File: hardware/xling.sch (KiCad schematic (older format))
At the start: 57 parts

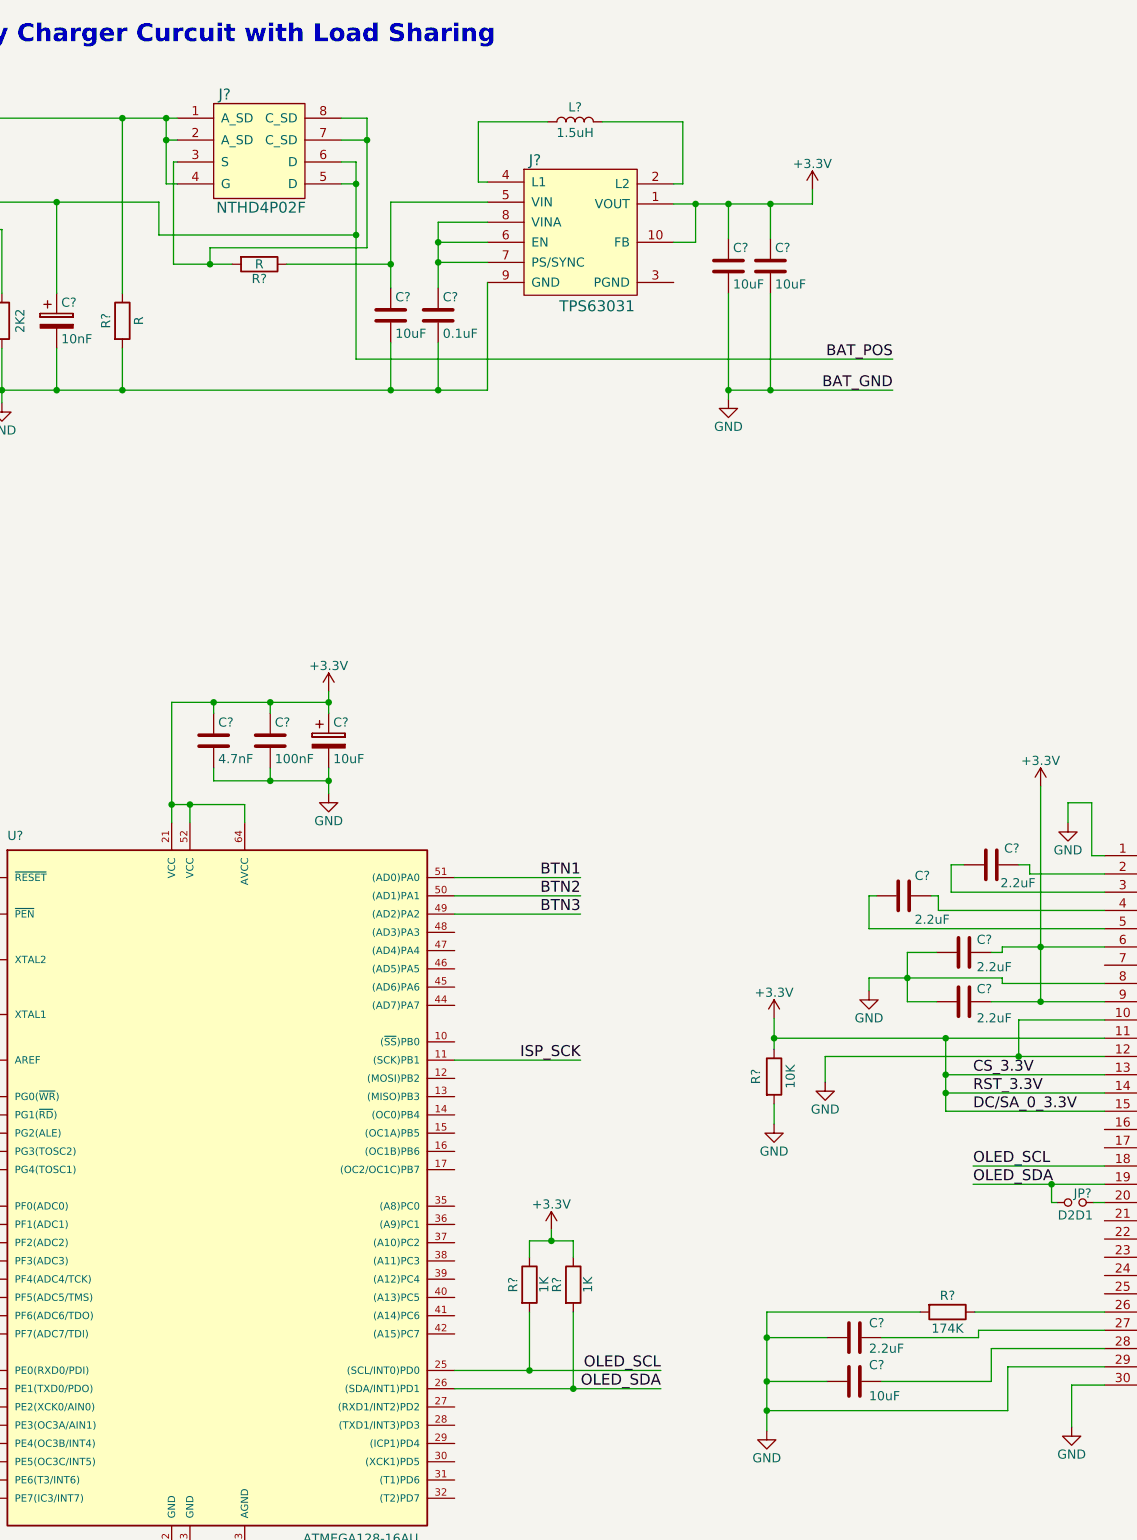
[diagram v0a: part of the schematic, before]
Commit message: patch 0.1.1: Add missing component values in schematic.
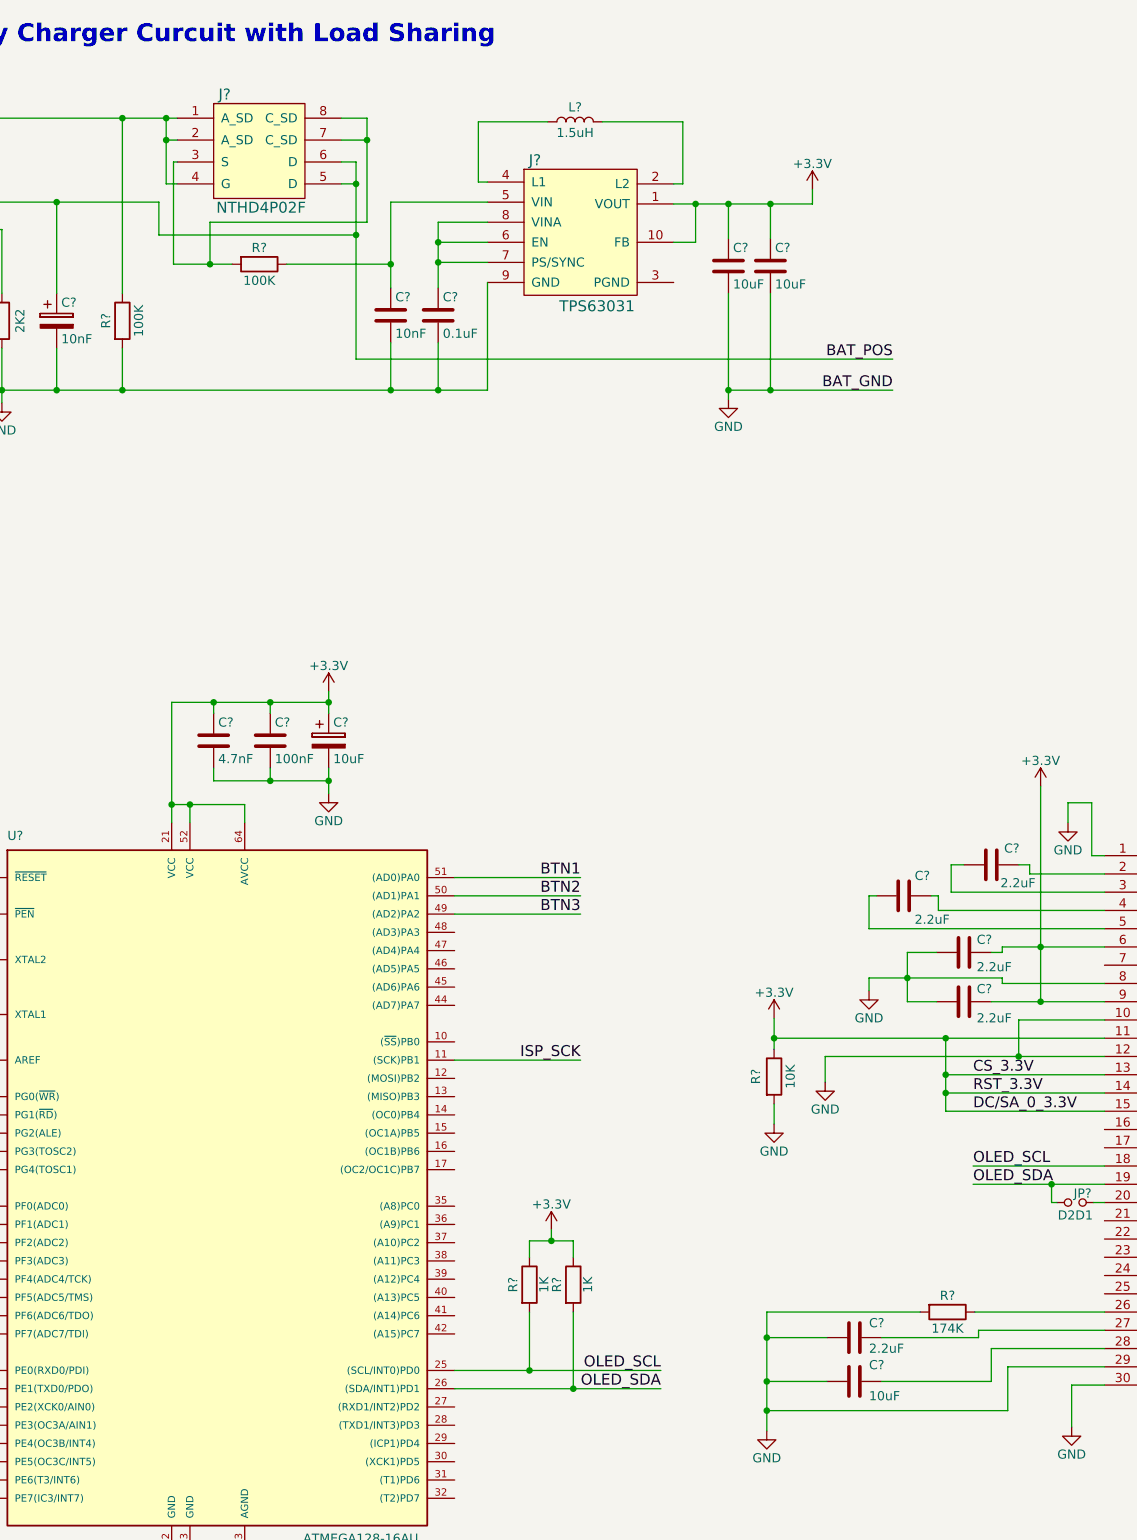
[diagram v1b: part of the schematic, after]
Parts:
- C?: value 10uF -> 10nF
- R? (x2): value R -> 100K

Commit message: patch 0.1.2: Schematic update with assigned footprints.
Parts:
- added J6: Battery, Pin_Headers:Pin_Header_Straight_1x02, symbol Conn_01x02
- C1, C17, C2, C9: renamed from C?; footprint (none) -> Capacitors_SMD:C_0805
- C10, C11, C12, C14, C16: renamed from C?; footprint (none) -> Capacitors_SMD:C_0603
- C13, C15, C18, C19, C20, C4, C7: renamed from C?; footprint (none) -> Capacitors_SMD:C_0402
- C3, C6: renamed from C?; value 10nF -> 4.7uF; footprint (none) -> Capacitors_SMD:CP_Elec_10x10
- C5, C8: renamed from C?; footprint (none) -> Capacitors_SMD:C_0201
- D1: renamed from D?; footprint (none) -> LEDs:LED_0603
- D2, D3: renamed from D?; footprint (none) -> LEDs:LED_0805
- D4: renamed from D?; value yellow -> amber; footprint (none) -> LEDs:LED_0603
- J4: renamed from J?; footprint (none) -> Connectors:USB_Mini-B
- J5: renamed from J?; footprint (none) -> Socket_Strips:Socket_Strip_Angled_2x03_Pitch2.54mm
- L1: renamed from L?; footprint (none) -> Inductors_SMD:L_1210
- R1, R17, R18, R19, R2, R3, R4, R5, R6, R7: renamed from R?; footprint (none) -> Resistors_SMD:R_1206
- R10: renamed from R?; footprint (none) -> Resistors_SMD:R_0805
- R11, R12, R13, R14, R15, R16, R8, R9: renamed from R?; footprint (none) -> Resistors_SMD:R_0603
- SW1, SW2, SW3, SW4: renamed from SW?; footprint (none) -> Buttons_Switches_THT:SW_PUSH_6mm
- gave numbers to parts that had none: 7
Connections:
- net GND: now also J6.2 (Pin_2)
- net BAT_POS: no longer names the net of C6.1, J1.5 (D), J1.6 (D), J3.3 (VBAT)
- net BAT_POS: now also J6.1 (Pin_1)

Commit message: patch 0.1.3: Add library with footprints.
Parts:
- JP1: footprint (none) -> Pin_Headers:Pin_Header_Straight_1x02
- Y1: footprint (none) -> Crystals:Crystal_HC49-SD_SMD
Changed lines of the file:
@@
 Title "Xling (Virtual Monster) Schematic"
 Date ""
-Rev "0.1.2"
+Rev "0.1.3"
 Comp ""
 Comment1 ""
@@
 F 0 "Y1" V 3060 6070 50  0000 C CNN
 F 1 "8MHz" V 2830 5830 50  0000 C CNN
-F 2 "" H 2840 6070 50  0001 C CNN
+F 2 "Crystals:Crystal_HC49-SD_SMD" H 2840 6070 50  0001 C CNN
 F 3 "" H 2840 6070 50  0001 C CNN
 	1    2840 6070
@@
 F 0 "JP1" H 9270 7200 50  0000 C CNN
 F 1 "D2D1" H 9310 7320 50  0000 C CNN
-F 2 "" H 9310 7250 50  0001 C CNN
+F 2 "Pin_Headers:Pin_Header_Straight_1x02" H 9310 7250 50  0001 C CNN
 F 3 "" H 9310 7250 50  0001 C CNN
 	1    9310 7250

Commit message: patch 0.1.4: Add footprint for MCP73831.
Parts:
- J3: footprint (none) -> Xling Footprints:MCP73831_SOT_23
- U1: footprint (none) -> Xling Footprints:Connector_FFC_FPC_MOLEX_524353071_30-pins
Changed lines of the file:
@@
 Title "Xling (Virtual Monster) Schematic"
 Date ""
-Rev "0.1.3"
+Rev "0.1.4"
 Comp ""
 Comment1 ""
@@
 F 0 "J3" H 2620 2220 60  0000 C CNN
 F 1 "MCP73831" H 2820 1620 60  0000 C CNN
-F 2 "" H 2820 1920 60  0001 C CNN
+F 2 "Xling Footprints:MCP73831_SOT_23" H 2820 1920 60  0001 C CNN
 F 3 "" H 2820 1920 60  0001 C CNN
 	1    2820 1920
@@
 F 0 "U1" H 9730 8200 60  0000 C CNN
 F 1 "SH1106G" H 11200 4990 60  0000 C CNN
-F 2 "" H 10820 7000 60  0001 C CNN
+F 2 "Xling Footprints:Connector_FFC_FPC_MOLEX_524353071_30-pins" H 10820 7000 60  0001 C CNN
 F 3 "" H 10820 7000 60  0001 C CNN
 	1    10520 6700

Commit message: patch 0.1.5: Add footprint for TPS63031.
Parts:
- J2: footprint (none) -> Xling Footprints:TPS63031_QFN_10
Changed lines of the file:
@@
 Title "Xling (Virtual Monster) Schematic"
 Date ""
-Rev "0.1.4"
+Rev "0.1.5"
 Comp ""
 Comment1 ""
@@
 F 0 "J2" H 6350 2260 60  0000 C CNN
 F 1 "TPS63031" H 6690 1460 60  0000 C CNN
-F 2 "" H 6470 1610 60  0001 C CNN
+F 2 "Xling Footprints:TPS63031_QFN_10" H 6470 1610 60  0001 C CNN
 F 3 "" H 6470 1610 60  0001 C CNN
 	1    6540 1900

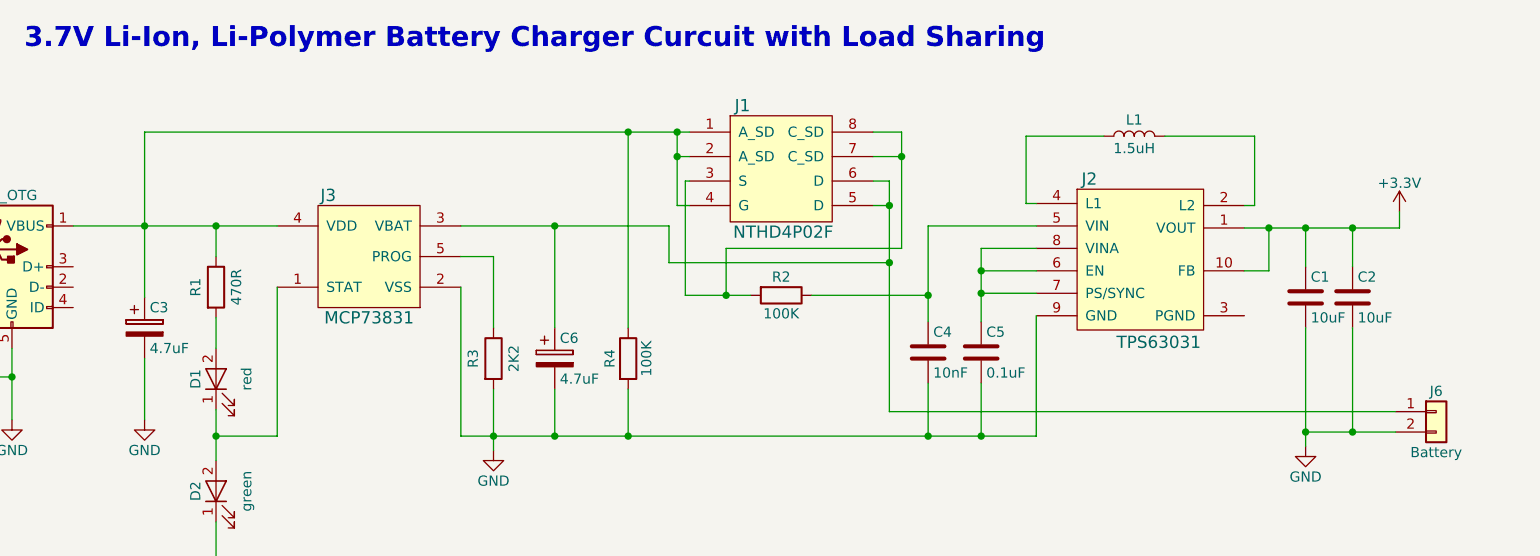
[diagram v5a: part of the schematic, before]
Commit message: patch 0.1.6: Add footprint for ATmega128L.
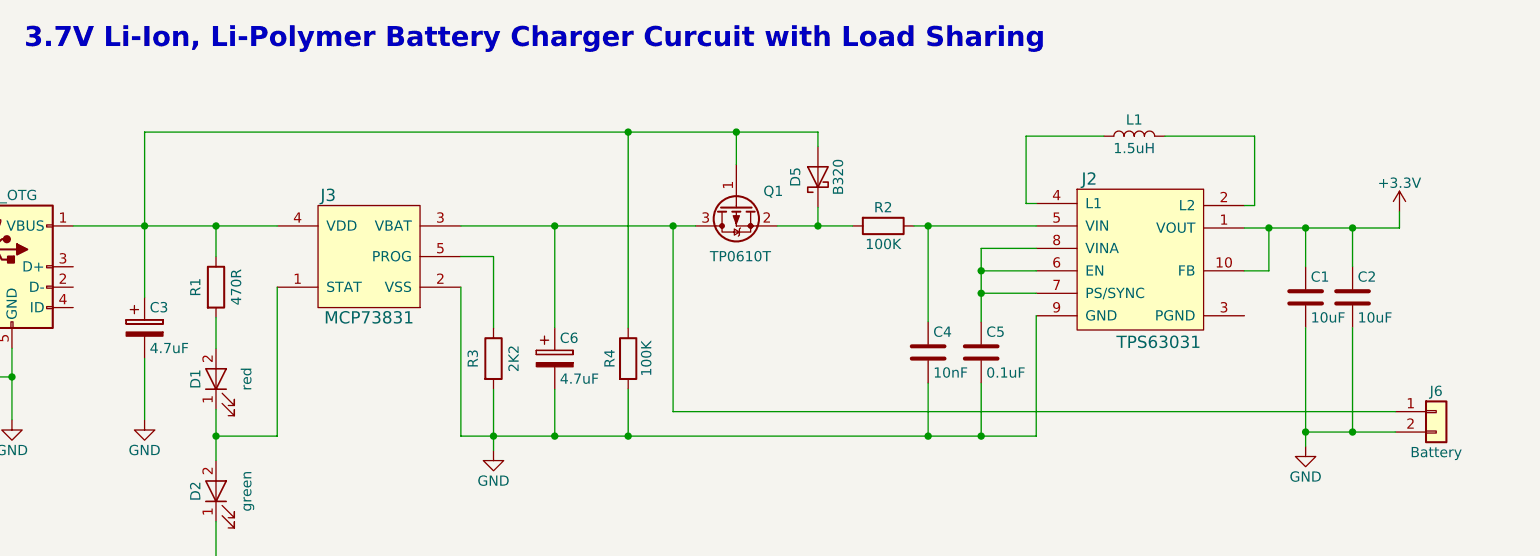
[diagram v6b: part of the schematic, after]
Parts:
- removed J1: NTHD4P02F, symbol NTHD4P02F
- added D5: B320, Diodes_SMD:SMC_Standard, symbol B320
- added Q1: TP0610T, TO_SOT_Packages_SMD:SOT-23, symbol TP0610T
- U2: footprint TQFP64 -> Xling Footprints:ATmega128_64-lead_14x14x1.0mm_TQFP
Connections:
- net at C6.1, J3.3 (VBAT), J6.1 (Pin_1): now also Q1.3 (D)
- net at C3.1, J3.4 (VDD), J4.1 (VBUS)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: now also D5.2 (A), Q1.1 (G)
- net at R2.2: now also D5.1 (K), Q1.2 (S)
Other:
- moved on the sheet: R2
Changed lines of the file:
@@
 Title "Xling (Virtual Monster) Schematic"
 Date ""
-Rev "0.1.5"
+Rev "0.1.6"
 Comp ""
 Comment1 ""
@@
 F 0 "U2" H 3460 9070 50  0000 L BNN
 F 1 "ATMEGA128-16AU" H 5080 5220 50  0000 L BNN
-F 2 "TQFP64" H 4610 7170 50  0001 C CIN
+F 2 "Xling Footprints:ATmega128_64-lead_14x14x1.0mm_TQFP" H 4610 7170 50  0001 C CIN
 F 3 "" H 4610 7170 50  0001 C CNN
 	1    4610 7170
@@
 L R R2
 U 1 1 59FE9BFF
-P 4840 2110
-F 0 "R2" V 4750 2110 50  0000 C CNN
-F 1 "100K" V 4930 2110 50  0000 C CNN
-F 2 "Resistors_SMD:R_1206" V 4770 2110 50  0001 C CNN
-F 3 "" H 4840 2110 50  0001 C CNN
-	1    4840 2110
+P 5340 1770
+F 0 "R2" V 5250 1770 50  0000 C CNN
+F 1 "100K" V 5430 1770 50  0000 C CNN
+F 2 "Resistors_SMD:R_1206" V 5270 1770 50  0001 C CNN
+F 3 "" H 5340 1770 50  0001 C CNN
+	1    5340 1770
 	0    1    1    0
 $EndComp
@@
 F 3 "" H 6440 7400 50  0001 C CNN
 	1    6440 7400
-	1    0    0    -1
-$EndComp
-$Comp
-L NTHD4P02F J1
-U 1 1 5A0054BD
-P 4830 1550
-F 0 "J1" H 4650 1920 60  0000 C CNN
-F 1 "NTHD4P02F" H 4850 1300 60  0000 C CNN
-F 2 "" H 4890 1470 60  0001 C CNN
-F 3 "" H 4890 1470 60  0001 C CNN
-	1    4830 1550
 	1    0    0    -1
 $EndComp
@@
 	7410 2270 7410 2850
 Wire Wire Line
-	5560 1770 6090 1770
+	5490 1770 6090 1770
 Wire Wire Line
 	5910 8270 7040 8270
@@
 	3730 1770 3730 2270
 Wire Wire Line
-	1720 1310 4390 1310
+	1720 1310 5020 1310
 Connection ~ 4090 1310
 Wire Wire Line
-	4390 1430 4330 1430
-Wire Wire Line
-	4330 1310 4330 1670
-Connection ~ 4330 1310
-Wire Wire Line
-	4330 1670 4390 1670
-Connection ~ 4330 1430
-Wire Wire Line
-	4390 1550 4370 1550
-Wire Wire Line
-	4370 1550 4370 2110
-Wire Wire Line
-	3270 1770 4290 1770
-Wire Wire Line
-	4290 1770 4290 1950
-Wire Wire Line
-	4290 1950 5370 1950
-Wire Wire Line
-	5370 1550 5370 2680
-Wire Wire Line
-	5370 1550 5290 1550
-Wire Wire Line
-	5290 1670 5370 1670
-Connection ~ 5370 1670
+	3270 1770 4420 1770
 Connection ~ 3730 1770
-Connection ~ 5370 1950
-Wire Wire Line
-	4370 2110 4690 2110
-Wire Wire Line
-	4990 2110 5560 2110
-Connection ~ 5560 2110
 Wire Wire Line
 	5560 1770 5560 2240
-Wire Wire Line
-	5290 1430 5430 1430
-Wire Wire Line
-	4570 1880 4570 2110
-Connection ~ 4570 2110
-Wire Wire Line
-	5290 1310 5430 1310
-Connection ~ 5430 1430
 Wire Wire Line
 	2460 5920 3310 5920
@@
 Connection ~ 9180 7150
 Wire Wire Line
-	5430 1880 4570 1880
-Wire Wire Line
-	5430 1310 5430 1880
-Wire Wire Line
 	7850 9330 7850 9530
 Wire Wire Line
@@
 Connection ~ 7640 2780
 Wire Wire Line
-	5370 2680 7850 2680
+	4310 2680 7850 2680
+$Comp
+L TP0610T Q1
+U 1 1 5A057EB3
+P 4620 1670
+F 0 "Q1" V 4550 1440 50  0000 L CNN
+F 1 "TP0610T" V 4870 1500 50  0000 L CNN
+F 2 "TO_SOT_Packages_SMD:SOT-23" H 4820 1595 50  0001 L CIN
+F 3 "" H 4620 1670 50  0001 L CNN
+	1    4620 1670
+	0    -1   1    0
+$EndComp
+Connection ~ 5560 1770
+Wire Wire Line
+	4620 1310 4620 1470
+Wire Wire Line
+	4820 1770 5190 1770
+Wire Wire Line
+	4310 2680 4310 1770
+Connection ~ 4310 1770
+$Comp
+L B320 D5
+U 1 1 5A05A5FD
+P 5020 1530
+F 0 "D5" H 5020 1640 50  0000 C CNN
+F 1 "B320" H 5020 1430 50  0000 C CNN
+F 2 "Diodes_SMD:SMC_Standard" H 5020 1355 50  0001 C CNN
+F 3 "" H 5020 1530 50  0001 C CNN
+	1    5020 1530
+	0    -1   -1   0
+$EndComp
+Wire Wire Line
+	5020 1310 5020 1380
+Connection ~ 4620 1310
+Wire Wire Line
+	5020 1680 5020 1770
+Connection ~ 5020 1770
 $EndSCHEMATC

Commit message: patch 0.1.7: Early prototype of the board.
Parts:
- J5: footprint Socket_Strips:Socket_Strip_Angled_2x03_Pitch2.54mm -> Socket_Strips:Socket_Strip_Straight_2x03_Pitch2.54mm
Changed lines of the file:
@@
 Title "Xling (Virtual Monster) Schematic"
 Date ""
-Rev "0.1.6"
+Rev "0.1.7"
 Comp ""
 Comment1 ""
@@
 F 0 "J5" H 4660 10480 50  0000 C CNN
 F 1 "AVR ISP" H 4660 10080 50  0000 C CNN
-F 2 "Socket_Strips:Socket_Strip_Angled_2x03_Pitch2.54mm" H 4610 10280 50  0001 C CNN
+F 2 "Socket_Strips:Socket_Strip_Straight_2x03_Pitch2.54mm" H 4610 10280 50  0001 C CNN
 F 3 "" H 4610 10280 50  0001 C CNN
 	1    4610 10280
